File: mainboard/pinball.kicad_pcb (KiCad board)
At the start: 2 copper layers, 83.8 x 48.3 mm, 86 parts, among them CON1 AVR-ISP-6, IC1 ATMEGA328-A, J1 Conn_01x14, J2 Conn_01x02, P1 SCREW_PLACEHOLDER, P2 SCREW_PLACEHOLDER, P3 SCREW_PLACEHOLDER, P4 SCREW_PLACEHOLDER, P5 PWR, P7 CONN_02X24, Q1 Q_NMOS_GDS, Q3 Q_NMOS_GDS, Q5 Q_NMOS_GDS, Q7 Q_NMOS_GDS, U1 R-78B5.0-2.0, U2 Teensy3.2, Y1 Crystal

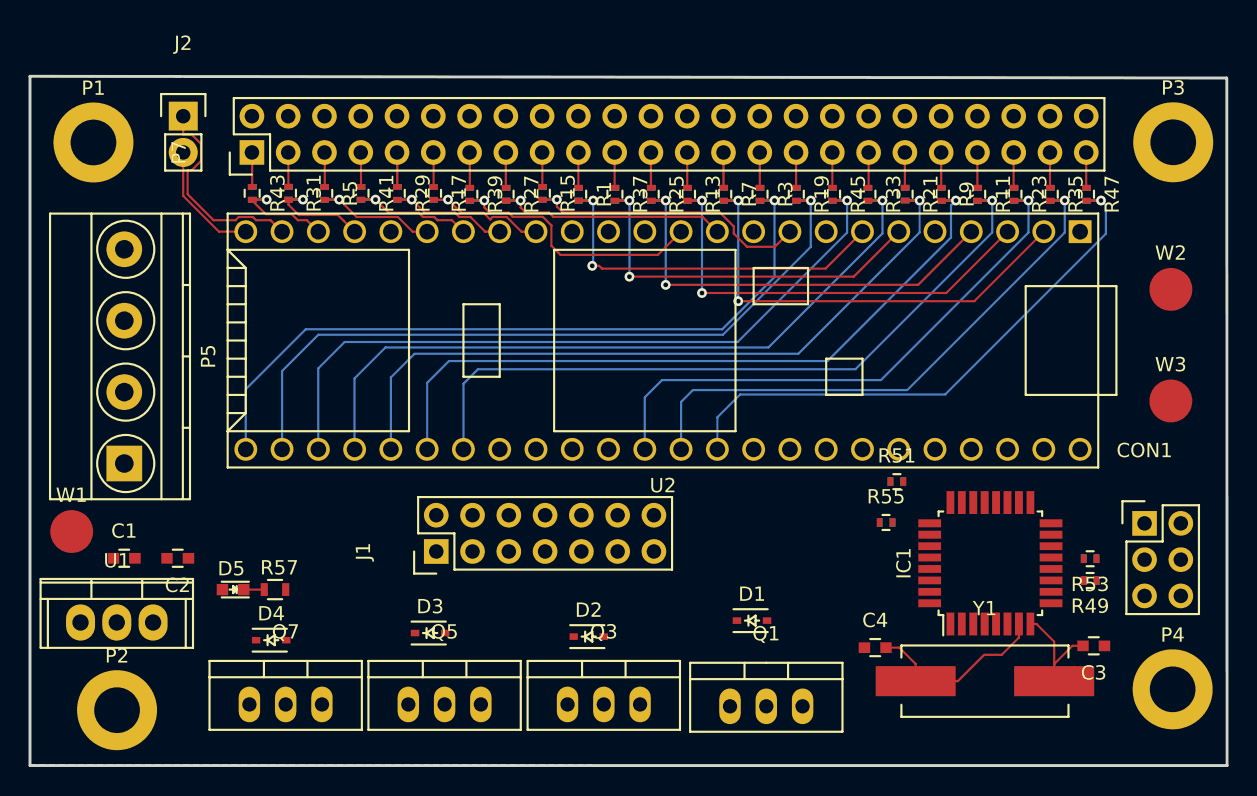
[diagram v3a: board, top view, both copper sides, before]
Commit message: Neopixel out. Lay out traces.
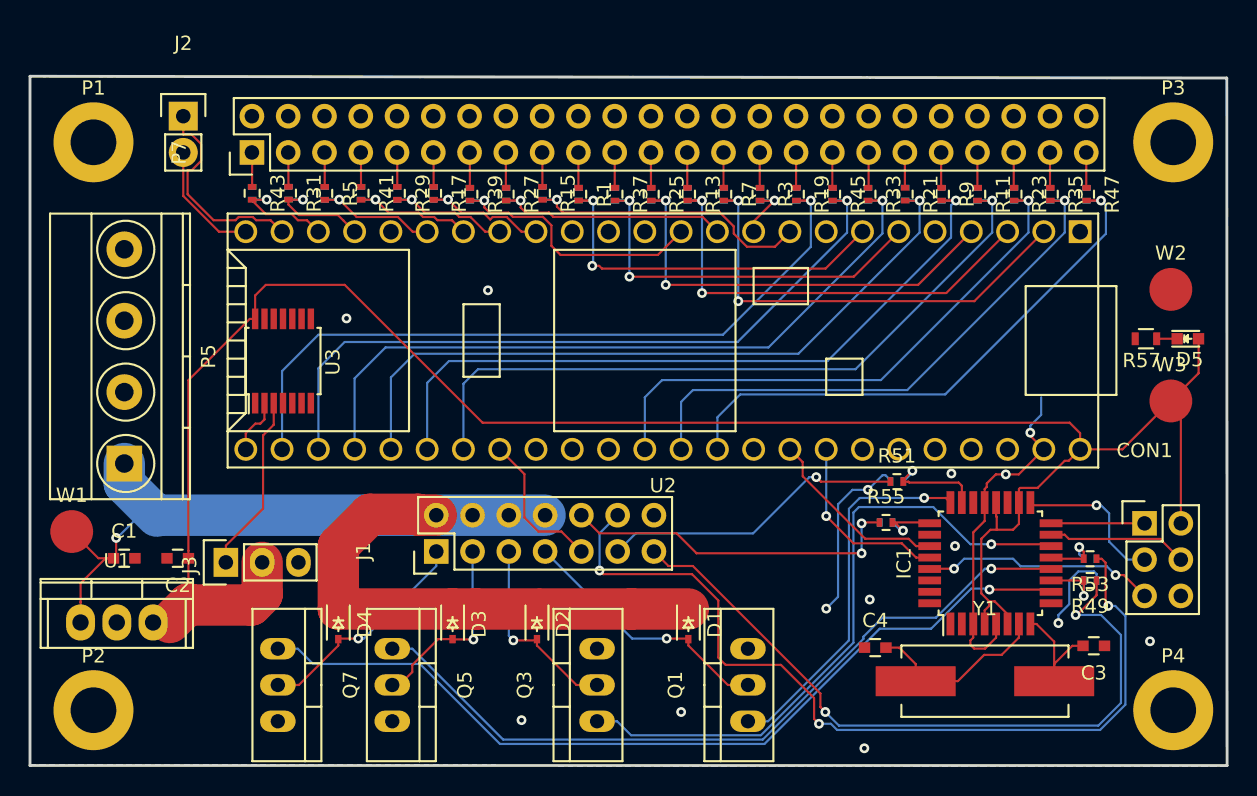
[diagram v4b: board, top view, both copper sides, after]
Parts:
- added J3: Conn_01x03_Male, Pin_Headers:Pin_Header_Straight_1x03, F.Cu at (89.9, 73.9)
- added U3: 74AHC125, Housings_SSOP:TSSOP-14_4.4x5mm_Pitch0.65mm, F.Cu at (93.9, 59.8)
- moved D5 69.1 mm to (157.3, 58.3), turned to 0 degrees
- moved R57 63.5 mm to (154.3, 58.3), turned to 180 degrees
- moved D4 4.84 mm to (97.8, 78.2), turned to 270 degrees
- moved D1 4.46 mm to (122.3, 78.2), turned to 270 degrees
- moved Q5 3.91 mm to (101.6, 82.5), turned to 270 degrees
- moved D2 3.73 mm to (111.7, 78.2), turned to 270 degrees
- moved Q1 1.97 mm to (126.5, 82.5), turned to 90 degrees
- moved D3 1.70 mm to (105.8, 78.2), turned to 270 degrees
- moved P2 1.65 mm to (80.6, 84.3)
- moved Q7 1.47 mm to (93.6, 82.5), turned to 270 degrees
- moved P4 1.46 mm to (156.2, 84.3)
- moved Q3 1.44 mm to (115.9, 82.5), turned to 90 degrees
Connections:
- U2 pad 10: (no net) -> SWITCH_LOW9
- U2 pad 30: SWITCH_LOW9 -> NEOPIXEL
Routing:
- net +5V: track 0.00 -> 141.3 mm
- net Vin: track 0.00 -> 84.1 mm, vias 0 -> 1
- net SCORE1: track 0.00 -> 61.5 mm, vias 0 -> 1
- net SCORE_ZERO_IN2: track 0.00 -> 61.3 mm, vias 0 -> 3
- net SCORE2: track 0.00 -> 53.8 mm, vias 0 -> 1
- net SCORE_ZERO_IN1: track 0.00 -> 50.6 mm, vias 0 -> 2
- net SWITCH_LOW9: track 51.9 -> 4.83 mm
- net SCORE3: track 0.00 -> 45.3 mm, vias 0 -> 1
- net GND: track 0.00 -> 42.7 mm, vias 0 -> 14
- net SCORE4: track 0.00 -> 26.2 mm, vias 0 -> 1
- net SCORE_ZERO_IN4: track 0.00 -> 24.1 mm, vias 0 -> 2
- net SCORE_ZERO_IN3: track 0.00 -> 21.4 mm, vias 0 -> 1
- net SCORE_OUT4A: track 0.00 -> 18.3 mm, vias 0 -> 1
- net RST: track 0.00 -> 16.4 mm, vias 0 -> 2
- net SCORE_OUT1A: track 0.00 -> 15.8 mm, vias 0 -> 1
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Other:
- net class Vin added: clearance 0.1524, trace_width 2.9, via_dia 0.6858, via_drill 0.3302
- board text added: "+"
- board text added: "GND"
- board text added: "S"

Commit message: Cleanup labels
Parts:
- renumbered W3 to +5V, W2 to GND, W1 to Vin
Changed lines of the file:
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@@
     (descr "Through hole pin header")
     (tags "pin header")
-    (fp_text reference J2 (at 0 -5.1) (layer F.SilkS)
+    (fp_text reference J2 (at 0 -5.1) (layer F.SilkS) hide
       (effects (font (size 1 1) (thickness 0.15)))
     )
@@
     (tags "capacitor 0603")
     (attr smd)
-    (fp_text reference C2 (at 0 -1.9 180) (layer F.SilkS)
+    (fp_text reference C2 (at 0.1855 1.6185 180) (layer F.SilkS)
       (effects (font (size 1 1) (thickness 0.15)))
     )
@@
     (tags "capacitor 0603")
     (attr smd)
-    (fp_text reference C3 (at 0 -1.9 180) (layer F.SilkS)
+    (fp_text reference C3 (at -1.27 -1.651 180) (layer F.SilkS)
       (effects (font (size 1 1) (thickness 0.15)))
     )
@@
     (tags "capacitor 0603")
     (attr smd)
-    (fp_text reference C4 (at 0 -1.9) (layer F.SilkS)
+    (fp_text reference C4 (at -1.3335 1.5875) (layer F.SilkS)
       (effects (font (size 1 1) (thickness 0.15)))
     )
@@
     (descr "Through hole pin header")
     (tags "pin header")
-    (fp_text reference CON1 (at 0 -5.1) (layer F.SilkS)
+    (fp_text reference CON1 (at 0 -5.1) (layer F.SilkS) hide
       (effects (font (size 1 1) (thickness 0.15)))
     )
@@
     (tags SOD-323)
     (attr smd)
-    (fp_text reference D1 (at 0 -1.85 270) (layer F.SilkS)
+    (fp_text reference D1 (at 2.667 0.889 270) (layer F.SilkS)
       (effects (font (size 1 1) (thickness 0.15)))
     )
@@
     (tags SOD-323)
     (attr smd)
-    (fp_text reference D2 (at 0 -1.85 270) (layer F.SilkS)
+    (fp_text reference D2 (at 2.8575 0.6985 270) (layer F.SilkS)
       (effects (font (size 1 1) (thickness 0.15)))
     )
@@
     (tags SOD-323)
     (attr smd)
-    (fp_text reference D3 (at 0 -1.85 270) (layer F.SilkS)
+    (fp_text reference D3 (at 2.54 -1.143 270) (layer F.SilkS)
       (effects (font (size 1 1) (thickness 0.15)))
     )
@@
     (tags SOD-323)
     (attr smd)
-    (fp_text reference D4 (at 0 -1.85 270) (layer F.SilkS)
+    (fp_text reference D4 (at 2.7305 -0.762 270) (layer F.SilkS)
       (effects (font (size 1 1) (thickness 0.15)))
     )
@@
     (descr "Mounting Hole 3.2mm, M3, DIN965")
     (tags "mounting hole 3.2mm m3 din965")
-    (fp_text reference P1 (at 0 -3.8) (layer F.SilkS)
+    (fp_text reference P1 (at 0 -3.8) (layer F.SilkS) hide
       (effects (font (size 1 1) (thickness 0.15)))
     )
@@
     (descr "Mounting Hole 3.2mm, M3, DIN965")
     (tags "mounting hole 3.2mm m3 din965")
-    (fp_text reference P2 (at 0 -3.8) (layer F.SilkS)
+    (fp_text reference P2 (at 0 -3.8) (layer F.SilkS) hide
       (effects (font (size 1 1) (thickness 0.15)))
     )
@@
     (descr "Mounting Hole 3.2mm, M3, DIN965")
     (tags "mounting hole 3.2mm m3 din965")
-    (fp_text reference P3 (at 0 -3.8) (layer F.SilkS)
+    (fp_text reference P3 (at 0 -3.8) (layer F.SilkS) hide
       (effects (font (size 1 1) (thickness 0.15)))
     )
@@
     (descr "Mounting Hole 3.2mm, M3, DIN965")
     (tags "mounting hole 3.2mm m3 din965")
-    (fp_text reference P4 (at 0 -3.8) (layer F.SilkS)
+    (fp_text reference P4 (at 0 -3.8) (layer F.SilkS) hide
       (effects (font (size 1 1) (thickness 0.15)))
     )
@@
     (at 82.804 66.9925 90)
     (descr "4-way 5mm pitch terminal block, Phoenix MKDS series")
-    (fp_text reference P5 (at 7.5 5.9 90) (layer F.SilkS)
+    (fp_text reference P5 (at 7.5 5.9 90) (layer F.SilkS) hide
       (effects (font (size 1 1) (thickness 0.15)))
     )
@@
     (descr "TO-220, Neutral, Vertical,")
     (tags "TO-220, Neutral, Vertical,")
-    (fp_text reference Q3 (at 0 -5.08 90) (layer F.SilkS)
+    (fp_text reference Q3 (at 0 -5.08 90) (layer F.SilkS) hide
       (effects (font (size 1 1) (thickness 0.15)))
     )
@@
     (descr "TO-220, Neutral, Vertical,")
     (tags "TO-220, Neutral, Vertical,")
-    (fp_text reference Q5 (at 0 -5.08 270) (layer F.SilkS)
+    (fp_text reference Q5 (at 0 -5.08 270) (layer F.SilkS) hide
       (effects (font (size 1 1) (thickness 0.15)))
     )
@@
     (descr "TO-220, Neutral, Vertical,")
     (tags "TO-220, Neutral, Vertical,")
-    (fp_text reference Q7 (at 0 -5.08 270) (layer F.SilkS)
+    (fp_text reference Q7 (at 0 -5.08 270) (layer F.SilkS) hide
       (effects (font (size 1 1) (thickness 0.15)))
     )
@@
     (descr "Mesurement Point, Round, SMD Pad, DM 3mm,")
     (tags "Mesurement Point, Round, SMD Pad, DM 3mm,")
-    (fp_text reference W1 (at 0 -2.54) (layer F.SilkS)
+    (fp_text reference Vin (at -0.6985 2.3495) (layer F.SilkS)
       (effects (font (size 1 1) (thickness 0.15)))
     )
@@
     (descr "Mesurement Point, Round, SMD Pad, DM 3mm,")
     (tags "Mesurement Point, Round, SMD Pad, DM 3mm,")
-    (fp_text reference W2 (at 0 -2.54) (layer F.SilkS)
+    (fp_text reference GND (at 0 -2.54) (layer F.SilkS)
       (effects (font (size 1 1) (thickness 0.15)))
     )
@@
     (descr "Mesurement Point, Round, SMD Pad, DM 3mm,")
     (tags "Mesurement Point, Round, SMD Pad, DM 3mm,")
-    (fp_text reference W3 (at 0 -2.54) (layer F.SilkS)
+    (fp_text reference +5V (at -3.302 0.8255) (layer F.SilkS)
       (effects (font (size 1 1) (thickness 0.15)))
     )
@@
     (tags "Crystal, Quarz, HC49-SD, SMD,")
     (attr smd)
-    (fp_text reference Y1 (at 0 -5.08) (layer F.SilkS)
+    (fp_text reference Y1 (at -0.0635 2.0955) (layer F.SilkS) hide
       (effects (font (size 1 1) (thickness 0.15)))
     )
@@
     (descr "TO-220, Neutral, Vertical,")
     (tags "TO-220, Neutral, Vertical,")
-    (fp_text reference Q1 (at 0 -5.08 90) (layer F.SilkS)
+    (fp_text reference Q1 (at 0 -5.08 90) (layer F.SilkS) hide
       (effects (font (size 1 1) (thickness 0.15)))
     )
@@
     (tags "resistor 0402")
     (attr smd)
-    (fp_text reference R51 (at 0 -1.8) (layer F.SilkS)
+    (fp_text reference R51 (at -2.471 -0.1905) (layer F.SilkS)
       (effects (font (size 1 1) (thickness 0.15)))
     )
@@
     (tags "resistor 0402")
     (attr smd)
-    (fp_text reference R52 (at 0 1.8 180) (layer B.SilkS)
+    (fp_text reference R52 (at 2.471 0.1905 180) (layer B.SilkS)
       (effects (font (size 1 1) (thickness 0.15)) (justify mirror))
     )
@@
     (tags "resistor 0402")
     (attr smd)
-    (fp_text reference R55 (at 0 -1.8) (layer F.SilkS)
+    (fp_text reference R55 (at -2.4075 0.0635) (layer F.SilkS)
       (effects (font (size 1 1) (thickness 0.15)))
     )
@@
     (tags "resistor 0402")
     (attr smd)
-    (fp_text reference R56 (at 0 1.8 180) (layer B.SilkS)
+    (fp_text reference R56 (at 2.413 -0.0635 180) (layer B.SilkS)
       (effects (font (size 1 1) (thickness 0.15)) (justify mirror))
     )
@@
     (descr "Through hole pin header")
     (tags "pin header")
-    (fp_text reference J3 (at -0.1905 -2.54 90) (layer F.SilkS)
+    (fp_text reference J3 (at -0.1905 -2.54 90) (layer F.SilkS) hide
       (effects (font (size 1 1) (thickness 0.15)))
     )
@@
     )
   )
-  (gr_text S (at 90.551 71.247 90) (layer B.Paste)
+  (gr_text S (at 89.5985 71.247 90) (layer B.Paste)
     (effects (font (size 1.5 1.5) (thickness 0.3)))
   )
-  (gr_text GND (at 95.9485 70.231 90) (layer B.Paste)
+  (gr_text GND (at 95.1865 70.231 90) (layer B.Paste)
     (effects (font (size 1.5 1.5) (thickness 0.3)))
   )
-  (gr_text + (at 93.0275 71.247) (layer B.Paste)
+  (gr_text + (at 92.583 71.3105) (layer B.Paste)
     (effects (font (size 1.5 1.5) (thickness 0.3)))
   )

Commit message: Digikey BOM
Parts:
- added REF**: bodgery, logo:bodgery, F.Cu at (119.6, 62.7)

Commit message: Remove 5V regulator. Power directly from MOLEX connector instead. Add CC-BY-SA license.
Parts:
- removed +5V, GND, Vin: TEST_1P, Measurement_Points:Measurement_Point_Round-SMD-Pad_Big
- removed C1, C2: 10uF, Capacitors_SMD:C_0603
- removed U1: R-78B5.0-2.0, Power_Integrations:TO-220
- added W1: TEST_1P, Measurement_Points:Measurement_Point_Round-SMD-Pad_Big, F.Cu at (82.0, 73.7)
- added W2: TEST_1P, Measurement_Points:Measurement_Point_Round-SMD-Pad_Big, F.Cu at (153.9, 51.6)
- added W3: TEST_1P, Measurement_Points:Measurement_Point_Round-SMD-Pad_Big, F.Cu at (157.5, 54.0)
- REF**: moved to B.Cu
- moved REF** 18.7 mm to (103.6, 53.1)
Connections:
- P5 pad 4: (no net) -> +5V
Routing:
- net +5V: track 141.3 -> 160.3 mm
- net Vin: track 84.1 -> 77.8 mm, vias 1 -> 0
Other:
- board text added: "RX"
- board text added: "TX"
- board text added: "v1 Copyright (c) 2019 Timm Murray CC-BY-SA 4.0"
